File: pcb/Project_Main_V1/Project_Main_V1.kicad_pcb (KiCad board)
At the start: 2 copper layers, 1 part, among them IC1 XC7Z007S-1CLG225C

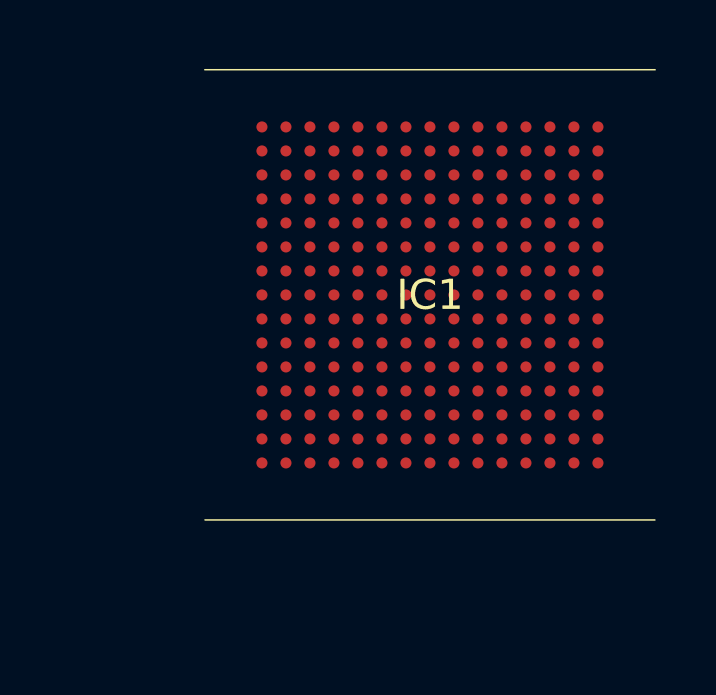
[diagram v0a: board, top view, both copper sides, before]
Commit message: Updated Schematics and Footprints of SOC
Updated Schematics and Footprints of SOC. The pitch is actually 0.8mm
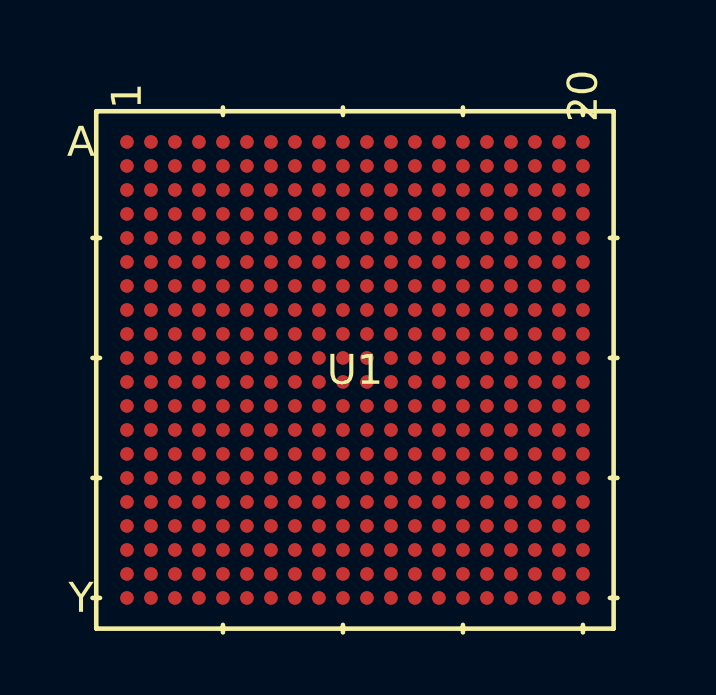
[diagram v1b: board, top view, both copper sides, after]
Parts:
- removed IC1: XC7Z007S-1CLG225C, XC7Z007S_1CLG225C:BGA225C80P15X15_1300X1300X150
- added U1: XC7Z010-1CLG400C, footprints:CLG400_AMD, F.Cu at (142.4, 100.9)
